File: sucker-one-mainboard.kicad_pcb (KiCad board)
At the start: 4 copper layers, 68 x 67.3 mm, 123 parts, among them J1 JST NC Valve, J10 BM10B-SRSS-TB(LF)(SN), J11 UART/SWD DNP, J12 TYPE-C-31-M-12, J2 JST NO Valve, J3 6P4C, J4 JST 3 Way Valve, J5 Jack-DC, J6 Phoenix Contact 1733570, J7 QWIIC I2C, J8 SPI, J9 BM04B-SRSS-TBT(LF)(SN), Q1 BSS138, Q2 BSS138, Q3 BSS138, Q4 STN4NF20L, Q5 BSS138, SW1 BOOTSEL, U1 LD1117S33TR, U2 TPS62112RSAR, U3 W25Q128JVPIQ TR, U4 RP2040, Y1 ABMM2-12.000MHZ-E2-T

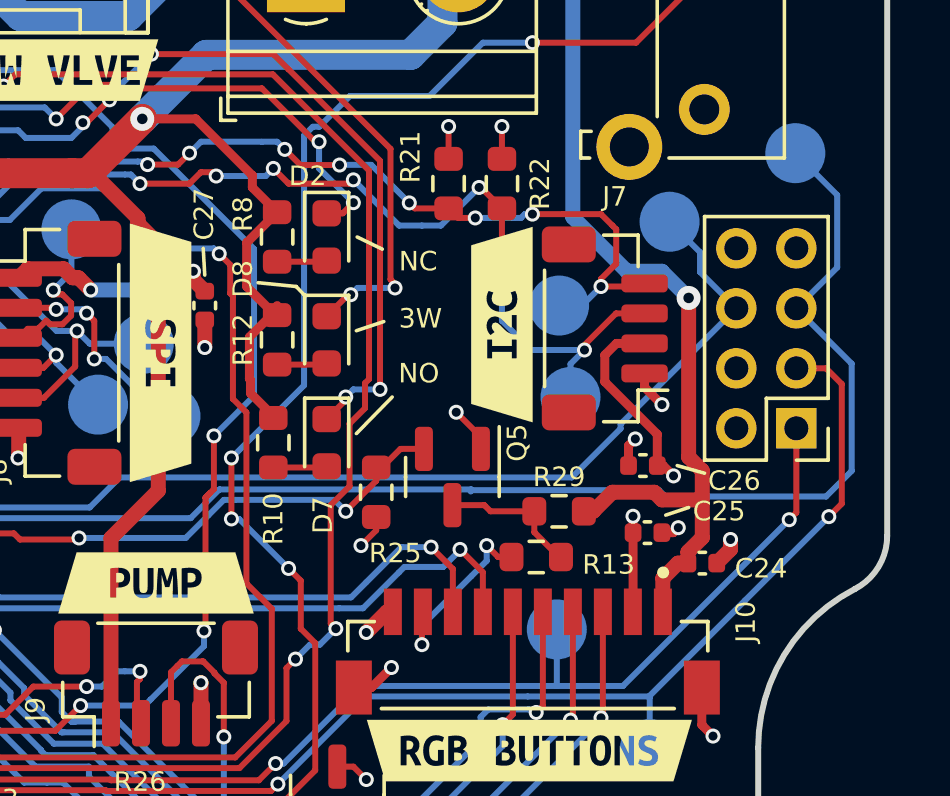
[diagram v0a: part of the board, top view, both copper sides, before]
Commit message: Update footprints and generate new iBOM
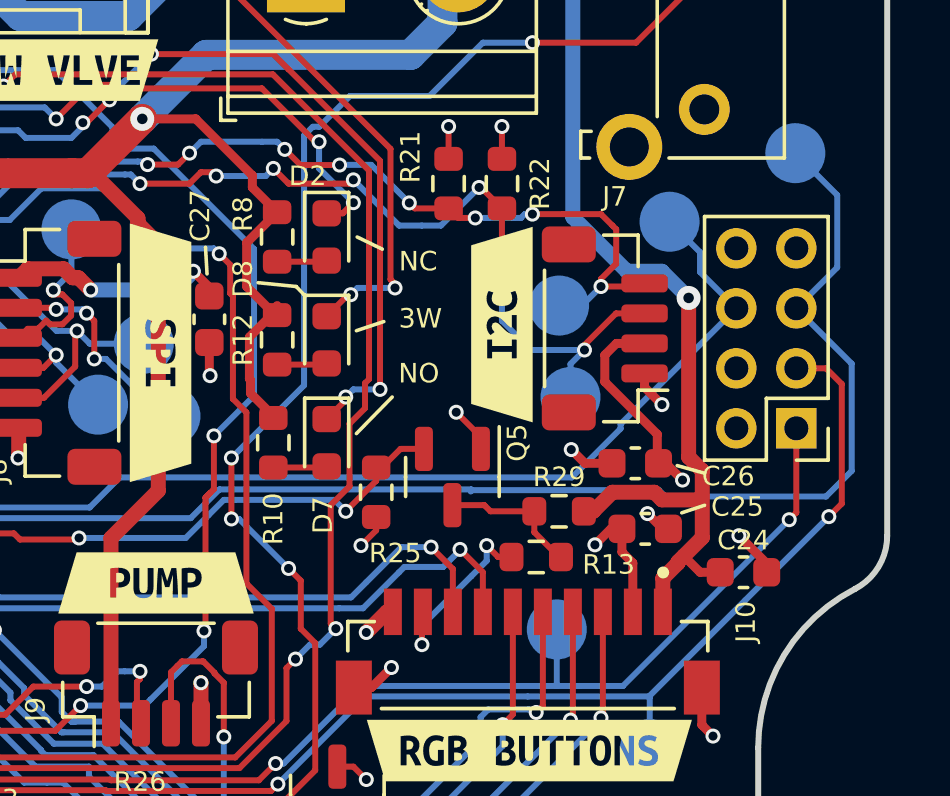
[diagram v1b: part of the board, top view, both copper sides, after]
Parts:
- C24, C25, C26, C27: footprint Capacitor_SMD:C_0402_1005Metric -> Capacitor_SMD:C_0603_1608Metric
- moved C24 1.41 mm to (129.2, 133.6)
- moved C27 0.48 mm to (111.4, 125.2)
- moved C26 0.27 mm to (125.6, 130.0)
- moved C25 0.15 mm to (125.9, 132.2)
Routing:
- net GND: track 58.1 -> 59.7 mm
- net +3V3: track 68.7 -> 70.3 mm
- net +5V: track 118.4 -> 119.6 mm

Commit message: Minor upgrades
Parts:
- C21: footprint Capacitor_SMD:C_0805_2012Metric -> Capacitor_SMD:C_0603_1608Metric
- L1: value L -> 6.8uH
- moved TP16 15.9 mm to (75.9, 129.2)
- moved C15 12.3 mm to (91.4, 143.1), turned to -90 degrees
- moved C22 12.3 mm to (101.5, 135.9), turned to 180 degrees
- moved C13 4.84 mm to (96.8, 145.2)
- moved C14 4.08 mm to (92.4, 143.0)
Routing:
- net +1V1: track 18.9 -> 31.6 mm, vias 4 -> 3
- net +5V: track 119.6 -> 129.0 mm
- net +3V3: track 70.3 -> 71.9 mm
- net GND: vias 90 -> 91

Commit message: Generate iBOM
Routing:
- net Net-(D7-Pad1): track 72.0 -> 73.4 mm
- net +5V: track 129.0 -> 130.0 mm
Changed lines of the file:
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@@
   (segment (start 90.31 129.54) (end 91.758 129.54) (width 0.25) (layer "F.Cu") (net 5))
   (segment (start 94.5134 131.2112) (end 94.5844 131.2112) (width 0.2) (layer "F.Cu") (net 6))
-  (segment (start 94.6606 131.2112) (end 94.7674 131.318) (width 0.2) (layer "F.Cu") (net 6))
   (segment (start 96.7994 144.2212) (end 96.7994 144.681) (width 0.2) (layer "F.Cu") (net 6))
   (segment (start 92.451 142.55) (end 93.300489 141.700511) (width 0.2) (layer "F.Cu") (net 6))
@@
   (segment (start 115.951 127.8635) (end 115.316 128.4985) (width 0.2) (layer "F.Cu") (net 13))
   (segment (start 91.8972 115.4938) (end 92.9639 116.5605) (width 0.5) (layer "F.Cu") (net 13))
-  (segment (start 85.6234 115.6462) (end 84.502398 115.6462) (width 0.5) (layer "F.Cu") (net 13))
+  (segment (start 84.502398 115.6462) (end 84.5058 115.6462) (width 0.5) (layer "F.Cu") (net 13))
   (segment (start 77.7725 105.915) (end 78.87 105.915) (width 0.5) (layer "F.Cu") (net 13))
   (segment (start 117.094 119.888) (end 117.094 120.015) (width 0.2) (layer "F.Cu") (net 13))
@@
   (segment (start 107.315 118.618) (end 108.077 117.856) (width 0.2) (layer "F.Cu") (net 13))
   (segment (start 76.2254 105.9688) (end 77.7187 105.9688) (width 0.2) (layer "F.Cu") (net 13))
+  (segment (start 84.5058 115.6462) (end 85.8012 116.9416) (width 0.5) (layer "F.Cu") (net 13))
+  (segment (start 86.1314 117.2718) (end 88.519 117.2718) (width 0.5) (layer "F.Cu") (net 13))
   (segment (start 109.474 116.332) (end 113.538 116.332) (width 0.2) (layer "F.Cu") (net 13))
   (segment (start 78.87 105.915) (end 80.264 104.521) (width 0.5) (layer "F.Cu") (net 13))
+  (segment (start 85.8012 116.9416) (end 86.1314 117.2718) (width 0.5) (layer "F.Cu") (net 13))
   (segment (start 113.538 116.332) (end 114.046 116.84) (width 0.2) (layer "F.Cu") (net 13))
   (segment (start 81.581398 112.7252) (end 80.264 112.7252) (width 0.5) (layer "F.Cu") (net 13))
@@
   (via (at 109.474 116.332) (size 0.5) (drill 0.3) (layers "F.Cu" "B.Cu") (net 13))
   (via (at 107.188 118.618) (size 0.5) (drill 0.3) (layers "F.Cu" "B.Cu") (net 13))
+  (via (at 88.519 117.2718) (size 0.5) (drill 0.3) (layers "F.Cu" "B.Cu") (net 13))
   (via (at 117.094 127.508) (size 0.5) (drill 0.3) (layers "F.Cu" "B.Cu") (net 13))
-  (via (at 85.6234 115.6462) (size 0.5) (drill 0.3) (layers "F.Cu" "B.Cu") (net 13))
   (via (at 102.108 118.872) (size 0.5) (drill 0.3) (layers "F.Cu" "B.Cu") (net 13))
   (segment (start 91.7448 115.6462) (end 91.8972 115.4938) (width 0.5) (layer "B.Cu") (net 13))
-  (segment (start 85.6234 115.6462) (end 90.0938 115.6462) (width 0.5) (layer "B.Cu") (net 13))
   (segment (start 105.283 119.126) (end 106.807 119.126) (width 0.2) (layer "B.Cu") (net 13))
   (segment (start 106.807 119.126) (end 107.188 118.745) (width 0.2) (layer "B.Cu") (net 13))
+  (segment (start 90.0938 115.697) (end 90.0938 115.6462) (width 0.5) (layer "B.Cu") (net 13))
   (segment (start 108.077 117.856) (end 108.077 117.729) (width 0.2) (layer "B.Cu") (net 13))
+  (segment (start 88.519 117.2718) (end 90.0938 115.697) (width 0.5) (layer "B.Cu") (net 13))
   (segment (start 102.108 118.872) (end 105.029 118.872) (width 0.2) (layer "B.Cu") (net 13))
   (segment (start 90.0938 115.6462) (end 91.7448 115.6462) (width 0.5) (layer "B.Cu") (net 13))
@@
   (segment (start 126.5216 134.922) (end 126.5216 133.803) (width 0.5) (layer "F.Cu") (net 79))
   (segment (start 84.7344 110.2868) (end 82.9564 112.0648) (width 0.5) (layer "F.Cu") (net 79))
-  (segment (start 81.153 116.5098) (end 81.153 115.824) (width 0.5) (layer "F.Cu") (net 79))
   (segment (start 127.0254 133.259388) (end 127.221394 133.063394) (width 0.5) (layer "F.Cu") (net 79))
   (segment (start 127.221394 133.063394) (end 127.836123 132.448665) (width 0.5) (layer "F.Cu") (net 79))
+  (segment (start 81.1276 113.411) (end 81.1276 116.4844) (width 0.5) (layer "F.Cu") (net 79))
   (segment (start 91.821 102.7176) (end 89.7128 102.7176) (width 0.5) (layer "F.Cu") (net 79))
-  (segment (start 81.153 115.824) (end 82.2452 114.7318) (width 0.5) (layer "F.Cu") (net 79))
+  (segment (start 81.1276 116.4844) (end 81.153 116.5098) (width 0.5) (layer "F.Cu") (net 79))
   (segment (start 127.0254 133.2992) (end 127.0254 133.259388) (width 0.5) (layer "F.Cu") (net 79))
   (segment (start 128.4348 133.604) (end 127.762 133.604) (width 0.3) (layer "F.Cu") (net 79))
@@
   (via (at 82.9564 112.0648) (size 0.8) (drill 0.35) (layers "F.Cu" "B.Cu") (net 79))
   (via (at 82.296 134.4676) (size 0.5) (drill 0.3) (layers "F.Cu" "B.Cu") (free) (net 79))
+  (via (at 81.1276 113.411) (size 0.5) (drill 0.3) (layers "F.Cu" "B.Cu") (net 79))
   (via (at 81.3308 133.5532) (size 0.5) (drill 0.3) (layers "F.Cu" "B.Cu") (free) (net 79))
   (via (at 81.1 127.3) (size 0.5) (drill 0.3) (layers "F.Cu" "B.Cu") (free) (net 79))
-  (via (at 82.2452 114.7318) (size 0.8) (drill 0.35) (layers "F.Cu" "B.Cu") (net 79))
   (via (at 81.3308 134.4676) (size 0.5) (drill 0.3) (layers "F.Cu" "B.Cu") (free) (net 79))
   (via (at 81.153 116.5098) (size 0.8) (drill 0.35) (layers "F.Cu" "B.Cu") (net 79))
@@
   (segment (start 126.492 123.571) (end 127.381 124.46) (width 0.5) (layer "B.Cu") (net 79))
   (segment (start 83.0072 112.1156) (end 82.9564 112.0648) (width 0.5) (layer "B.Cu") (net 79))
+  (segment (start 82.9564 112.0648) (end 81.3054 112.0648) (width 0.5) (layer "B.Cu") (net 79))
   (segment (start 80.8 126) (end 81.1 126.3) (width 0.5) (layer "B.Cu") (net 79))
+  (segment (start 81.3054 112.0648) (end 81.1276 112.2426) (width 0.5) (layer "B.Cu") (net 79))
   (segment (start 85.6234 106.9594) (end 85.6234 110.2868) (width 0.5) (layer "B.Cu") (net 79))
   (segment (start 68.1736 123.1392) (end 71.3344 126.3) (width 0.5) (layer "B.Cu") (net 79))
   (segment (start 91.821 102.7176) (end 92.0242 102.9208) (width 0.5) (layer "B.Cu") (net 79))
-  (segment (start 83.0072 113.9698) (end 83.0072 112.1156) (width 0.5) (layer "B.Cu") (net 79))
   (segment (start 80.7 126) (end 80.4 126.3) (width 0.5) (layer "B.Cu") (net 79))
+  (segment (start 81.1276 112.2426) (end 81.1276 113.411) (width 0.5) (layer "B.Cu") (net 79))
   (segment (start 68.9102 116.8654) (end 68.9102 119.6848) (width 0.5) (layer "B.Cu") (net 79))
   (segment (start 77.4446 129.1844) (end 79.329 127.3) (width 0.2) (layer "B.Cu") (net 79))
   (segment (start 118.364 108.331) (end 123.5202 113.4872) (width 0.5) (layer "B.Cu") (net 79))
   (segment (start 75.9206 129.1844) (end 77.4446 129.1844) (width 0.2) (layer "B.Cu") (net 79))
-  (segment (start 82.2452 114.7318) (end 83.0072 113.9698) (width 0.5) (layer "B.Cu") (net 79))
   (segment (start 71.3344 126.3) (end 80.4 126.3) (width 0.5) (layer "B.Cu") (net 79))
   (segment (start 123.5202 113.4872) (end 123.5202 114.2492) (width 0.5) (layer "B.Cu") (net 79))

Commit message: Changed part no and regenerated iBOM
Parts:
- J7: value QWIIC I2C -> BM04B-SRSS-TBT(LF)(SN)
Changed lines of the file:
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@@
       (effects (font (size 0.65 0.65) (thickness 0.13)))
     )
-    (fp_text value "QWIIC I2C" (at 0 3.3 90) (layer "F.Fab")
+    (fp_text value "BM04B-SRSS-TBT(LF)(SN)" (at 0 3.3 90) (layer "F.Fab")
       (effects (font (size 1 1) (thickness 0.15)))
     )
